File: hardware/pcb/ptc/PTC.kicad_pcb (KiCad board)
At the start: 2 copper layers, 29 x 29 mm, 10 parts, among them J1 Conn_01x03, SW1 SW_SP3T

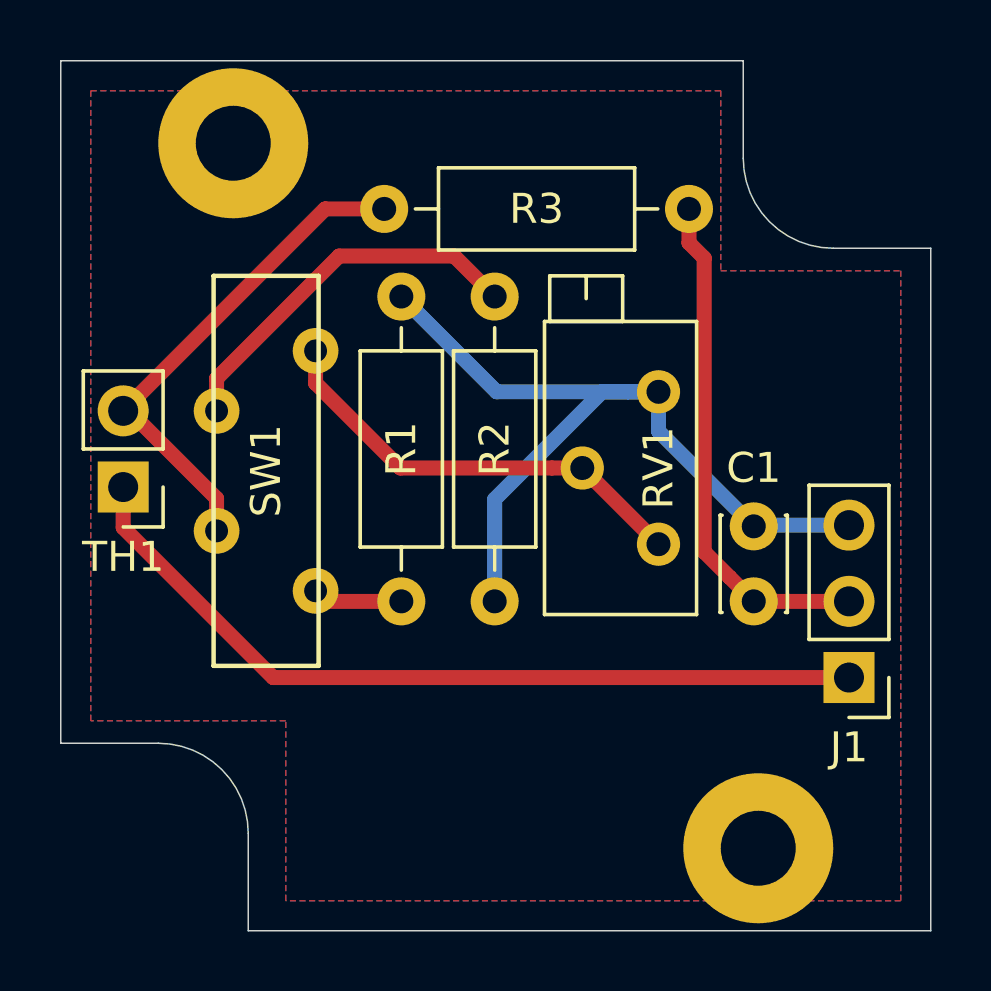
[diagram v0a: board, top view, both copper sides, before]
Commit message: feat: General PCB improvements
redo PTC pcb

Issue #14
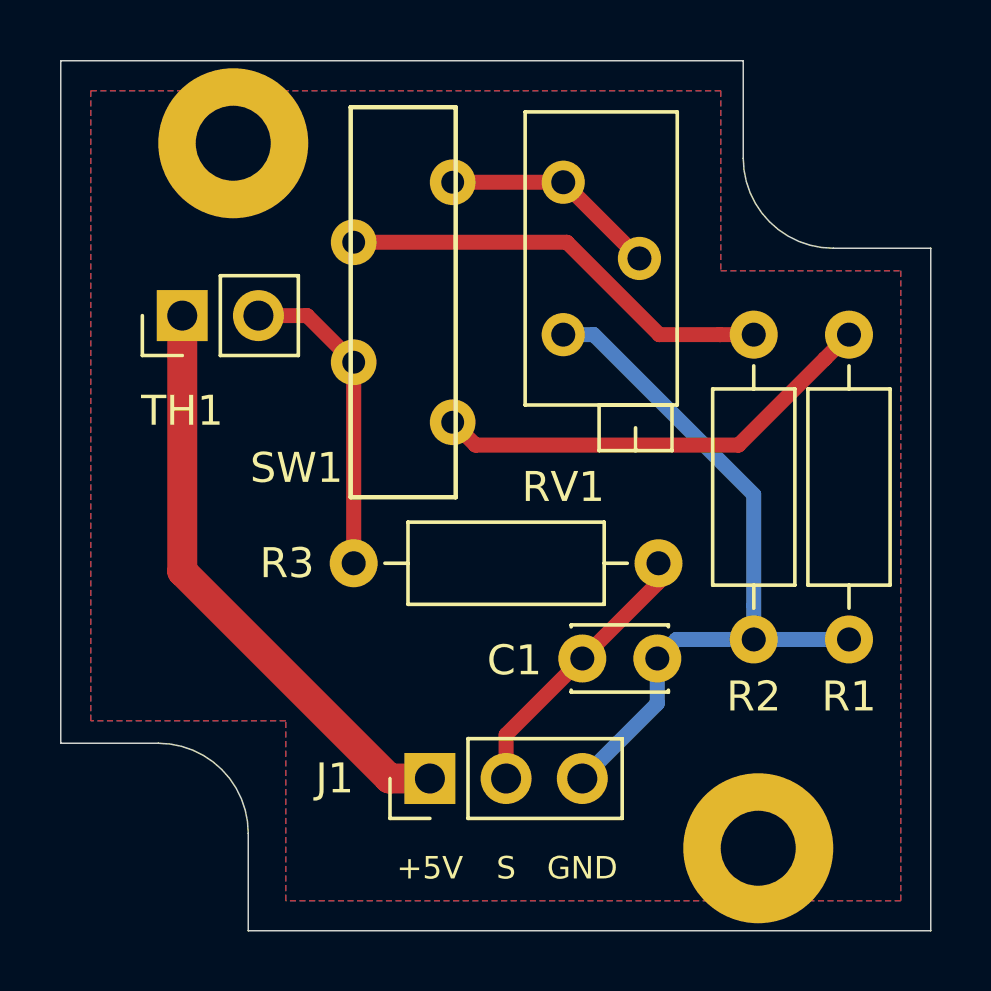
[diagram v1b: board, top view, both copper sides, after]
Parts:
- moved R1 17.4 mm to (41.3, 24.1), turned to 270 degrees
- moved J1 14.4 mm to (27.3, 38.9), turned to 90 degrees
- moved RV1 12.5 mm to (31.8, 19.1), turned to 90 degrees
- moved R3 11.9 mm to (24.8, 31.8)
- moved R2 8.73 mm to (38.1, 24.1)
- moved SW1 7.24 mm to (26.4, 23.1)
- moved TH1 6.04 mm to (19.1, 23.5), turned to 90 degrees
- moved C1 6.02 mm to (32.4, 34.9), turned to 0 degrees
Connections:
- net Net-(C1-Pad1) renamed /SIGNAL
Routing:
- net Net-(R1-Pad1): track 3.00 -> 15.1 mm
- net +5V: track 27.6 -> 19.6 mm
- net /SIGNAL: track 17.2 -> 9.28 mm
- net Net-(RV1-Pad1): track 14.7 -> 7.28 mm
- net Net-(R3-Pad1): track 16.9 -> 10.5 mm
- net GND: track 29.2 -> 25.1 mm
- net Net-(R2-Pad1): track 12.6 -> 14.6 mm
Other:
- board text added: "+5V"
- board text added: "GND"
- board text added: "S"
